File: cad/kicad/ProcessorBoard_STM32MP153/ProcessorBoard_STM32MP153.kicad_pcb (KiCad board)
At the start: 6 copper layers, 50 x 50 mm, 7 parts, among them IC401 IS43LD16320A-25BLI, J501 SFP, U201 STM32MP153CACx

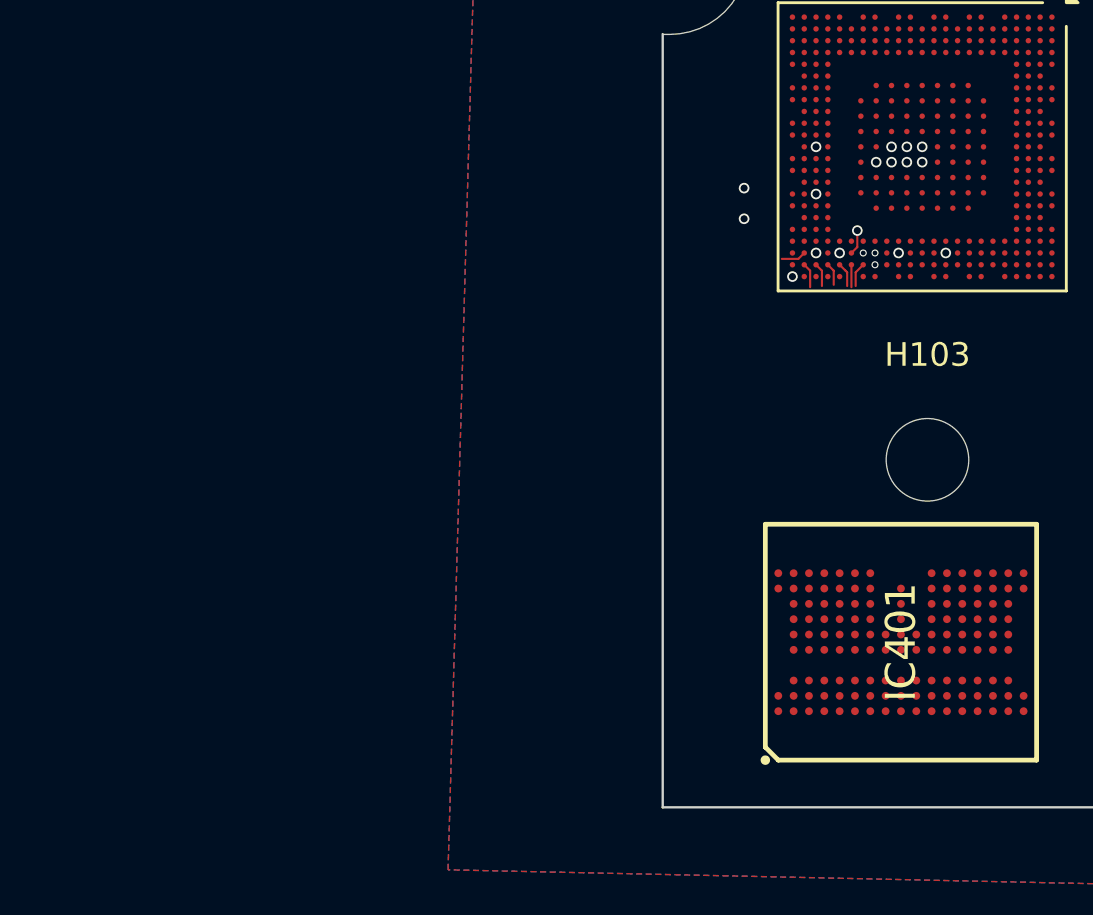
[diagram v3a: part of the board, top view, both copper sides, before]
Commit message: mpu power connections
about mpu, apparently onboard usb supply has a requirement for the onboard ldo's to be happy, so u have to tap out 2 deticated pins. and theres also a power off sequence as well???
1v8 life looking better every day, 3v3(>2v9) trenches over there
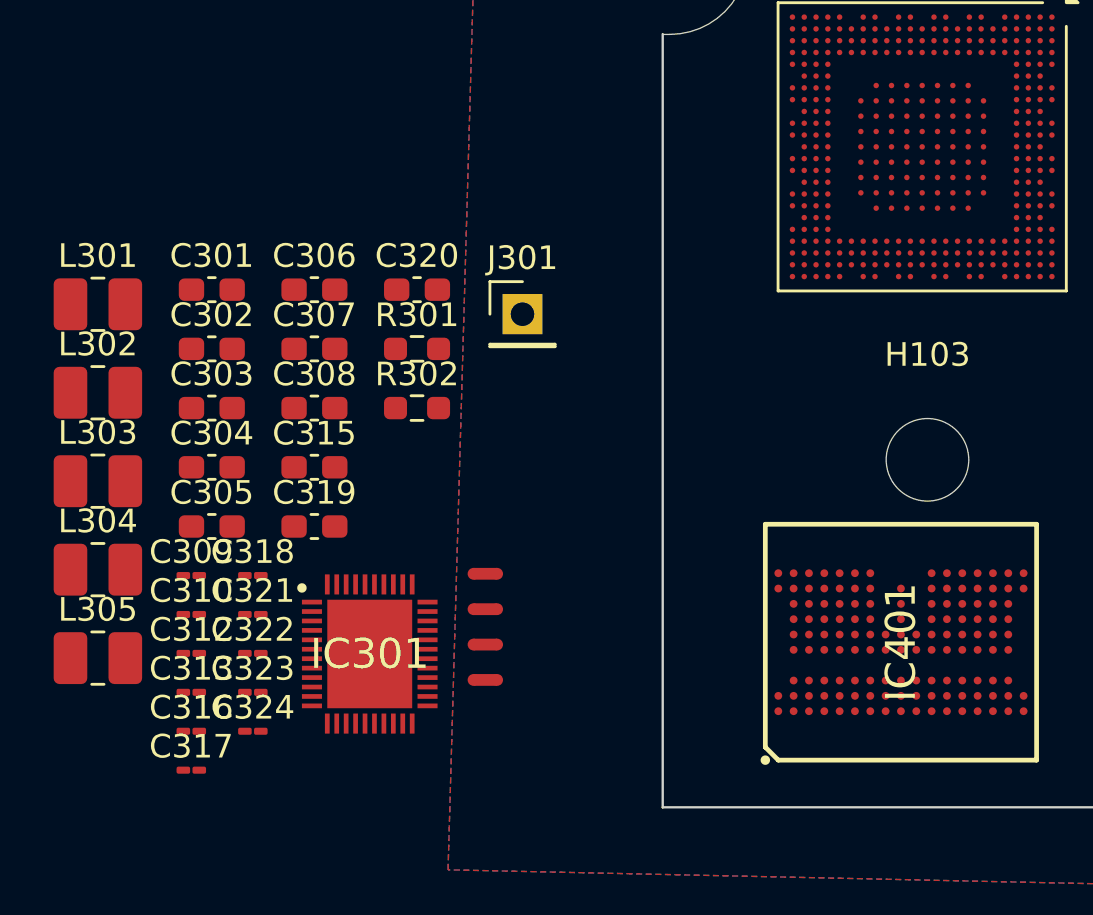
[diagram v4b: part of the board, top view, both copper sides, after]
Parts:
- added C301: 10u, Capacitor_SMD:C_0603_1608Metric_Pad1.08x0.95mm_HandSolder, F.Cu at (110.9, 98.1)
- added C302: 22u, Capacitor_SMD:C_0603_1608Metric_Pad1.08x0.95mm_HandSolder, F.Cu at (110.9, 100.6)
- added C303: 10u, Capacitor_SMD:C_0603_1608Metric_Pad1.08x0.95mm_HandSolder, F.Cu at (110.9, 103.1)
- added C304: 22u, Capacitor_SMD:C_0603_1608Metric_Pad1.08x0.95mm_HandSolder, F.Cu at (110.9, 105.6)
- added C305: 10u, Capacitor_SMD:C_0603_1608Metric_Pad1.08x0.95mm_HandSolder, F.Cu at (110.9, 108.1)
- added C306: 22u, Capacitor_SMD:C_0603_1608Metric_Pad1.08x0.95mm_HandSolder, F.Cu at (115.2, 98.1)
- added C307: 10u, Capacitor_SMD:C_0603_1608Metric_Pad1.08x0.95mm_HandSolder, F.Cu at (115.2, 100.6)
- added C308: 22u, Capacitor_SMD:C_0603_1608Metric_Pad1.08x0.95mm_HandSolder, F.Cu at (115.2, 103.1)
- added C309: 1u, Capacitor_SMD:C_01005_0402Metric_Pad0.57x0.30mm_HandSolder, F.Cu at (110.0, 110.2)
- added C310: 4.7u, Capacitor_SMD:C_01005_0402Metric_Pad0.57x0.30mm_HandSolder, F.Cu at (110.0, 111.8)
- added C312: 1u, Capacitor_SMD:C_01005_0402Metric_Pad0.57x0.30mm_HandSolder, F.Cu at (110.0, 113.5)
- added C313: 4.7u, Capacitor_SMD:C_01005_0402Metric_Pad0.57x0.30mm_HandSolder, F.Cu at (110.0, 115.1)
- added C315: 10u, Capacitor_SMD:C_0603_1608Metric_Pad1.08x0.95mm_HandSolder, F.Cu at (115.2, 105.6)
- added C316: 1u, Capacitor_SMD:C_01005_0402Metric_Pad0.57x0.30mm_HandSolder, F.Cu at (110.0, 116.8)
- added C317: 1u, Capacitor_SMD:C_01005_0402Metric_Pad0.57x0.30mm_HandSolder, F.Cu at (110.0, 118.4)
- added C318: 4.7u, Capacitor_SMD:C_01005_0402Metric_Pad0.57x0.30mm_HandSolder, F.Cu at (112.6, 110.2)
- added C319: 10u, Capacitor_SMD:C_0603_1608Metric_Pad1.08x0.95mm_HandSolder, F.Cu at (115.2, 108.1)
- added C320: 10u, Capacitor_SMD:C_0603_1608Metric_Pad1.08x0.95mm_HandSolder, F.Cu at (119.6, 98.1)
- added C321: 1u, Capacitor_SMD:C_01005_0402Metric_Pad0.57x0.30mm_HandSolder, F.Cu at (112.6, 111.8)
- added C322: 4.7u, Capacitor_SMD:C_01005_0402Metric_Pad0.57x0.30mm_HandSolder, F.Cu at (112.6, 113.5)
- added C323: 4.7u, Capacitor_SMD:C_01005_0402Metric_Pad0.57x0.30mm_HandSolder, F.Cu at (112.6, 115.1)
- added C324: 1u, Capacitor_SMD:C_01005_0402Metric_Pad0.57x0.30mm_HandSolder, F.Cu at (112.6, 116.8)
- added IC301: STPMIC1BPQR, __WM_Local:QFN40P500X600X80-45N-D, F.Cu at (117.6, 113.5)
- added J301: Conn_01x01_Pin, Connector_PinHeader_2.54mm:PinHeader_1x01_P2.54mm_Vertical, F.Cu at (124.1, 99.1)
- added L301: 1u, Inductor_SMD:L_1008_2520Metric_Pad1.43x2.20mm_HandSolder, F.Cu at (106.1, 98.7)
- added L302: 1u, Inductor_SMD:L_1008_2520Metric_Pad1.43x2.20mm_HandSolder, F.Cu at (106.1, 102.4)
- added L303: 1u, Inductor_SMD:L_1008_2520Metric_Pad1.43x2.20mm_HandSolder, F.Cu at (106.1, 106.2)
- added L304: 1u, Inductor_SMD:L_1008_2520Metric_Pad1.43x2.20mm_HandSolder, F.Cu at (106.1, 109.9)
- added L305: 1u, Inductor_SMD:L_1008_2520Metric_Pad1.43x2.20mm_HandSolder, F.Cu at (106.1, 113.7)
- added NT301: NetTie_2, NetTie:NetTie-2_SMD_Pad0.5mm, F.Cu at (122.5, 110.1)
- added NT302: NetTie_2, NetTie:NetTie-2_SMD_Pad0.5mm, F.Cu at (122.5, 111.6)
- added NT303: NetTie_2, NetTie:NetTie-2_SMD_Pad0.5mm, F.Cu at (122.5, 113.1)
- added NT304: NetTie_2, NetTie:NetTie-2_SMD_Pad0.5mm, F.Cu at (122.5, 114.6)
- added R301: 3090, Resistor_SMD:R_0603_1608Metric_Pad0.98x0.95mm_HandSolder, F.Cu at (119.6, 100.6)
- added R302: 3090, Resistor_SMD:R_0603_1608Metric_Pad0.98x0.95mm_HandSolder, F.Cu at (119.6, 103.1)
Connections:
- U201 pad 1G2: unconnected-(U201-VDD_ANA-Pad1G2) -> /V_{dd_core}
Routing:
- net GND: track 1.05 -> 0.00 mm, vias 13 -> 0
- net unconnected-(U201-DDR_DQ26-PadAB21): track 1.05 -> 0.00 mm
- net unconnected-(U201-DDR_DQS3P-PadAB22): track 1.05 -> 0.00 mm
- net unconnected-(U201-DDR_DQS1P-PadU22): track 1.03 -> 0.00 mm
- net unconnected-(U201-DDR_DQ14-PadW22): track 1.03 -> 0.00 mm
- net unconnected-(U201-DDR_DQ31-PadAA22): track 1.00 -> 0.00 mm
- net unconnected-(U201-DDR_DQ25-PadY22): track 0.95 -> 0.00 mm
- net unconnected-(U201-DDR_DQM1-PadV22): track 0.95 -> 0.00 mm
- net unconnected-(U201-DDR_DQ8-PadT21): track 0.88 -> 0.00 mm, vias 1 -> 0
- net unconnected-(U201-DDR_DQ9-PadU21): track 0.85 -> 0.00 mm, vias 1 -> 0
- net unconnected-(U201-DDR_DQ11-PadW21): vias 1 -> 0
- net unconnected-(U201-DDR_DQ10-PadT22): vias 1 -> 0
- net /V_{dd_core}: vias 3 -> 0

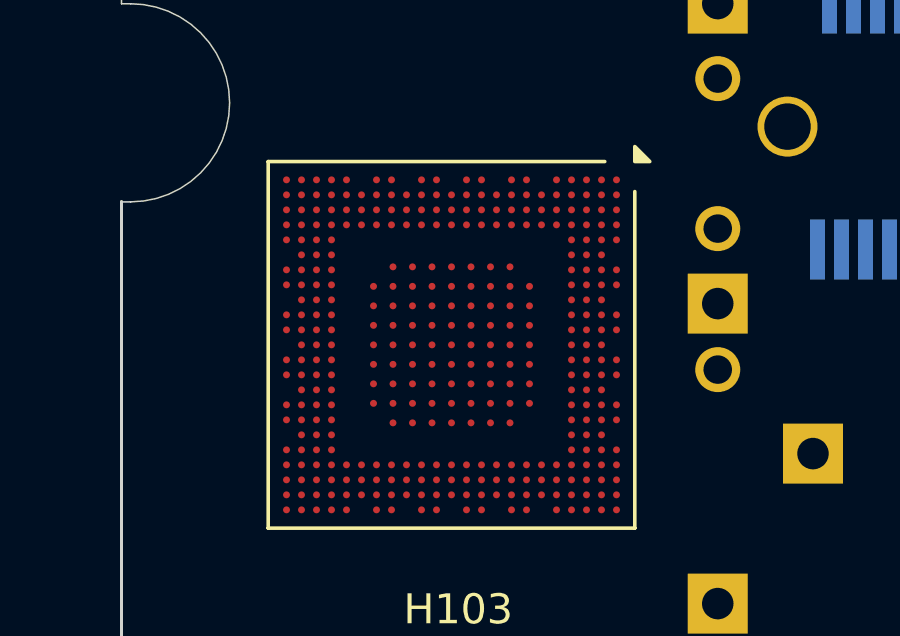
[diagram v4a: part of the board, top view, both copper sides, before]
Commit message: mr przudent get down
a thrid DDR voltage requirement has hit the power plane.
the cost of 11$ ram is apparently 3 distinct power nets :( .
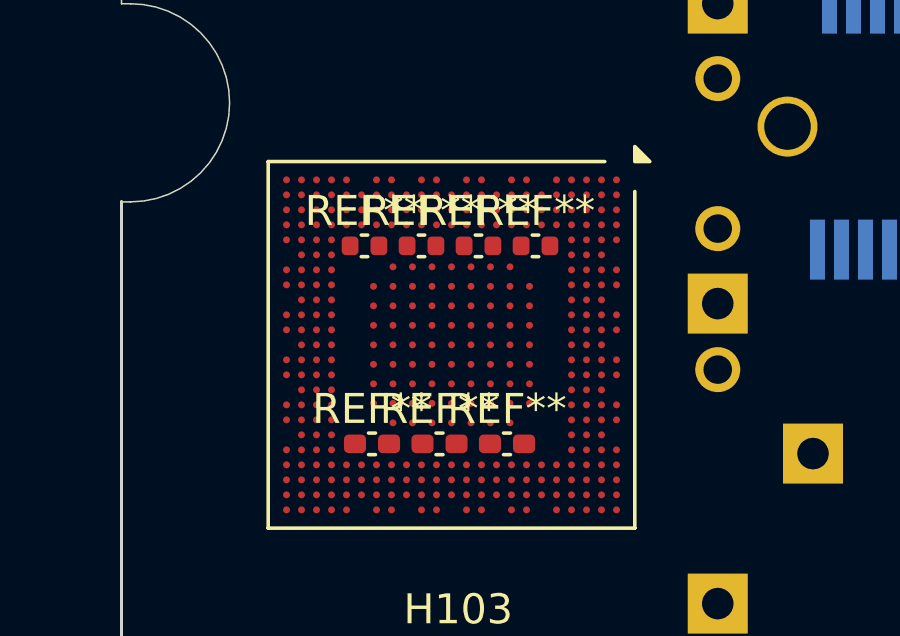
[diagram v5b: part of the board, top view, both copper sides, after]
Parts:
- added REF**: C_0402_1005Metric, Capacitor_SMD:C_0402_1005Metric, F.Cu at (143.8, 88.7)
- added REF**: C_0402_1005Metric_Pad0.74x0.62mm_HandSolder, Capacitor_SMD:C_0402_1005Metric_Pad0.74x0.62mm_HandSolder, F.Cu at (142.8, 95.3)
- added REF**: C_0402_1005Metric, Capacitor_SMD:C_0402_1005Metric, F.Cu at (141.9, 88.7)
- added REF**: C_0402_1005Metric_Pad0.74x0.62mm_HandSolder, Capacitor_SMD:C_0402_1005Metric_Pad0.74x0.62mm_HandSolder, F.Cu at (138.3, 95.3)
- added REF**: C_0402_1005Metric, Capacitor_SMD:C_0402_1005Metric, F.Cu at (140.0, 88.7)
- added REF**: C_0402_1005Metric, Capacitor_SMD:C_0402_1005Metric, F.Cu at (138.1, 88.7)
- added REF**: C_0402_1005Metric_Pad0.74x0.62mm_HandSolder, Capacitor_SMD:C_0402_1005Metric_Pad0.74x0.62mm_HandSolder, F.Cu at (140.6, 95.3)

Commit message: is this tuff
most datasheets from LCSC are "not for public release"
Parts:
- removed H103: MountingHole, MountingHole:MountingHole_3.5mm
- removed REF** (x4): C_0402_1005Metric, Capacitor_SMD:C_0402_1005Metric
- removed REF** (x3): C_0402_1005Metric_Pad0.74x0.62mm_HandSolder, Capacitor_SMD:C_0402_1005Metric_Pad0.74x0.62mm_HandSolder
- added C201: 100n, Capacitor_SMD:C_0402_1005Metric_Pad0.74x0.62mm_HandSolder, F.Cu at (111.7, 96.7)
- added C202: 1u, Capacitor_SMD:C_0402_1005Metric_Pad0.74x0.62mm_HandSolder, F.Cu at (106.1, 81.3)
- added C203: 1u, Capacitor_SMD:C_0402_1005Metric_Pad0.74x0.62mm_HandSolder, F.Cu at (106.1, 82.9)
- added C204: 1u, Capacitor_SMD:C_0402_1005Metric_Pad0.74x0.62mm_HandSolder, F.Cu at (106.1, 84.6)
- added C205: 1u, Capacitor_SMD:C_0402_1005Metric_Pad0.74x0.62mm_HandSolder, F.Cu at (106.1, 86.2)
- added C206: 1u, Capacitor_SMD:C_0402_1005Metric_Pad0.74x0.62mm_HandSolder, F.Cu at (106.1, 87.9)
- added C207: 1u, Capacitor_SMD:C_0402_1005Metric_Pad0.74x0.62mm_HandSolder, F.Cu at (106.1, 89.5)
- added C208: 1u, Capacitor_SMD:C_0402_1005Metric_Pad0.74x0.62mm_HandSolder, F.Cu at (108.7, 79.6)
- added C209: 1u, Capacitor_SMD:C_0402_1005Metric_Pad0.74x0.62mm_HandSolder, F.Cu at (108.7, 81.3)
- added C210: 1u, Capacitor_SMD:C_0402_1005Metric_Pad0.74x0.62mm_HandSolder, F.Cu at (108.7, 82.9)
- added C211: 1u, Capacitor_SMD:C_0402_1005Metric_Pad0.74x0.62mm_HandSolder, F.Cu at (108.7, 84.6)
- added C212: 1u, Capacitor_SMD:C_0402_1005Metric_Pad0.74x0.62mm_HandSolder, F.Cu at (108.7, 86.2)
- added C213: 1u, Capacitor_SMD:C_0402_1005Metric_Pad0.74x0.62mm_HandSolder, F.Cu at (108.7, 87.9)
- added C214: 1u, Capacitor_SMD:C_0402_1005Metric_Pad0.74x0.62mm_HandSolder, F.Cu at (108.7, 89.5)
- added C215: 1u, Capacitor_SMD:C_0402_1005Metric_Pad0.74x0.62mm_HandSolder, F.Cu at (111.3, 79.6)
- added C216: 1u, Capacitor_SMD:C_0402_1005Metric_Pad0.74x0.62mm_HandSolder, F.Cu at (111.3, 81.3)
- added C217: 1u, Capacitor_SMD:C_0402_1005Metric_Pad0.74x0.62mm_HandSolder, F.Cu at (111.3, 82.9)
- added C218: 1u, Capacitor_SMD:C_0402_1005Metric_Pad0.74x0.62mm_HandSolder, F.Cu at (111.3, 84.6)
- added C219: 1n, Capacitor_SMD:C_0402_1005Metric_Pad0.74x0.62mm_HandSolder, F.Cu at (111.3, 86.2)
- added C220: 1n, Capacitor_SMD:C_0402_1005Metric_Pad0.74x0.62mm_HandSolder, F.Cu at (111.3, 87.9)
- added C221: 1u, Capacitor_SMD:C_0402_1005Metric_Pad0.74x0.62mm_HandSolder, F.Cu at (111.3, 89.5)
- added C222: 1u, Capacitor_SMD:C_0402_1005Metric_Pad0.74x0.62mm_HandSolder, F.Cu at (113.9, 79.6)
- added C223: 1u, Capacitor_SMD:C_0402_1005Metric_Pad0.74x0.62mm_HandSolder, F.Cu at (113.9, 81.3)
- added C224: 100n, Capacitor_SMD:C_0402_1005Metric_Pad0.74x0.62mm_HandSolder, F.Cu at (111.7, 98.7)
- added C225: 100n, Capacitor_SMD:C_0402_1005Metric_Pad0.74x0.62mm_HandSolder, F.Cu at (114.1, 83.1)
- added C227: 100n, Capacitor_SMD:C_0402_1005Metric_Pad0.74x0.62mm_HandSolder, F.Cu at (114.1, 85.1)
- added C228: 100n, Capacitor_SMD:C_0402_1005Metric_Pad0.74x0.62mm_HandSolder, F.Cu at (111.7, 100.6)
- added C229: 100n, Capacitor_SMD:C_0402_1005Metric_Pad0.74x0.62mm_HandSolder, F.Cu at (114.1, 87.1)
- added C401: 100n, Capacitor_SMD:C_0402_1005Metric_Pad0.74x0.62mm_HandSolder, F.Cu at (114.6, 109.3)
- added C402: 100n, Capacitor_SMD:C_0402_1005Metric_Pad0.74x0.62mm_HandSolder, F.Cu at (114.6, 111.3)
- added C403: 100n, Capacitor_SMD:C_0402_1005Metric_Pad0.74x0.62mm_HandSolder, F.Cu at (114.6, 113.3)
- added C404: 100n, Capacitor_SMD:C_0402_1005Metric_Pad0.74x0.62mm_HandSolder, F.Cu at (114.6, 115.2)
- added J201: Conn_01x03_Pin, Connector_PinHeader_1.27mm:PinHeader_1x03_P1.27mm_Vertical, F.Cu at (117.3, 90.5)
- added R201: 47k, Resistor_SMD:R_0603_1608Metric_Pad0.98x0.95mm_HandSolder, F.Cu at (117.4, 80.1)
- added R202: 47k, Resistor_SMD:R_0603_1608Metric_Pad0.98x0.95mm_HandSolder, F.Cu at (117.4, 82.6)
- added R203: 3090, Resistor_SMD:R_0603_1608Metric_Pad0.98x0.95mm_HandSolder, F.Cu at (117.4, 85.1)
- added R204: 47k, Resistor_SMD:R_0603_1608Metric_Pad0.98x0.95mm_HandSolder, F.Cu at (117.4, 87.6)
- added R205: 240, Capacitor_SMD:C_0402_1005Metric_Pad0.74x0.62mm_HandSolder, F.Cu at (110.0, 91.3)
- added R206: 10k, Capacitor_SMD:C_0402_1005Metric_Pad0.74x0.62mm_HandSolder, F.Cu at (142.8, 84.5)
- added R207: 1k, Capacitor_SMD:C_0402_1005Metric_Pad0.74x0.62mm_HandSolder, F.Cu at (142.8, 86.4)
- added R208: 10, Resistor_SMD:R_0402_1005Metric_Pad0.72x0.64mm_HandSolder, F.Cu at (142.8, 85.4)
- added R401: 240, Capacitor_SMD:C_0402_1005Metric_Pad0.74x0.62mm_HandSolder, F.Cu at (110.4, 115.2)
- added TP201: TestPoint, TestPoint:TestPoint_Pad_D1.5mm, F.Cu at (106.6, 92.1)
- added X201: ECS-3225MVQ-240-CN-TR, Package_DFN_QFN:CDFN-4_2.5x3.2mm_P2.1mm, F.Cu at (138.8, 85.8)
- C309, C310, C312, C313, C316, C317, C318, C321, C322, C323, C324: footprint Capacitor_SMD:C_01005_0402Metric_Pad0.57x0.30mm_HandSolder -> Capacitor_SMD:C_0402_1005Metric_Pad0.74x0.62mm_HandSolder
- IC301: moved to B.Cu
- J501: footprint Connector:Connector_SFP_and_Cage -> __WM_Local:Connector_SFP_and_Cage; moved to F.Cu
- R301, R302: value 3090 -> 1.2k
- moved J301 61.0 mm to (163.5, 145.6)
- moved C307 56.2 mm to (160.1, 134.5)
- moved C312 56.2 mm to (154.8, 147.4)
- moved C313 56.2 mm to (154.8, 149.1)
- moved C319 56.2 mm to (160.1, 142.0)
- moved R301 56.2 mm to (164.4, 134.5)
- moved C306 56.2 mm to (160.1, 132.0)
- moved C308 56.2 mm to (160.1, 137.0)
- moved C309 56.2 mm to (154.8, 144.1)
- moved C310 56.2 mm to (154.8, 145.8)
- moved C315 56.2 mm to (160.1, 139.5)
- moved C316 56.2 mm to (154.8, 150.7)
- moved C317 56.2 mm to (154.8, 152.3)
- moved C320 56.2 mm to (164.4, 132.0)
- moved C322 56.2 mm to (157.4, 147.4)
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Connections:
- net /Power MPU/INTn renamed /INTn
- net /Power MPU/RSTn renamed /RSTn
- net /Power MPU/SCL renamed /SCL
- net /Power MPU/SDA renamed /SDA
- net /Power MPU/WakeUp renamed /WakeUp
- C319 pad 1: /V_{dd_core} -> /V_{dd_IO}
- C320 pad 1: /V_{dd_DDR2} -> /V_{dd_DDR1}
- IC301 pad 13: /V_{dd_core} -> /V_{dd_IO}
- IC301 pad 14: /V_{dd_DDR2} -> /V_{dd_DDR1}
- IC301 pad 44: /Power MPU/PwrCtrl -> /PwrCtrl
- IC401 pad B5: unconnected-(IC401-VDD2_1-PadB5) -> /V_{dd_DDRQ}
- IC401 pad B6: unconnected-(IC401-VDD1_1-PadB6) -> /V_{dd_DDR1}
- IC401 pad C1: unconnected-(IC401-VDD1_2-PadC1) -> /V_{dd_DDR1}
- IC401 pad C10: unconnected-(IC401-VDDQ_2-PadC10) -> /V_{dd_DDRQ}
- IC401 pad C2: unconnected-(IC401-VSS_1-PadC2) -> GND
- IC401 pad C5: unconnected-(IC401-VSS_2-PadC5) -> GND
- IC401 pad C6: unconnected-(IC401-VSSQ_1-PadC6) -> GND
- IC401 pad C7: unconnected-(IC401-VDDQ_1-PadC7) -> /V_{dd_DDRQ}
- IC401 pad C9: unconnected-(IC401-VSSQ_2-PadC9) -> GND
- IC401 pad D1: unconnected-(IC401-VSS_3-PadD1) -> GND
- IC401 pad D10: unconnected-(IC401-VSSQ_3-PadD10) -> GND
- IC401 pad D2: unconnected-(IC401-VDD2_2-PadD2) -> /V_{dd_DDRQ}
- IC401 pad D3: unconnected-(IC401-ZQ-PadD3) -> Net-(IC401-ZQ)
- IC401 pad D5: unconnected-(IC401-VDDQ_3-PadD5) -> /V_{dd_DDRQ}
- IC401 pad E1: unconnected-(IC401-VSSCA_1-PadE1) -> GND
- IC401 pad E10: unconnected-(IC401-VSSQ_4-PadE10) -> GND
- IC401 pad E2: unconnected-(IC401-CA9-PadE2) -> /a9
- IC401 pad E3: unconnected-(IC401-CA8-PadE3) -> /a8
- IC401 pad E8: unconnected-(IC401-DQ15-PadE8) -> /d15
- IC401 pad E9: unconnected-(IC401-VDDQ_4-PadE9) -> /V_{dd_DDRQ}
- IC401 pad F1: unconnected-(IC401-VDDCA_1-PadF1) -> /V_{dd_DDRQ}
- IC401 pad F10: unconnected-(IC401-VDDQ_5-PadF10) -> /V_{dd_DDRQ}
- IC401 pad F2: unconnected-(IC401-CA6-PadF2) -> /a6
- IC401 pad F3: unconnected-(IC401-CA7-PadF3) -> /a7
- IC401 pad F5: unconnected-(IC401-VSSQ_5-PadF5) -> GND
- IC401 pad F6: unconnected-(IC401-DQ11-PadF6) -> /d11
- IC401 pad F7: unconnected-(IC401-DQ13-PadF7) -> /d13
- IC401 pad F8: unconnected-(IC401-DQ14-PadF8) -> /d14
- IC401 pad F9: unconnected-(IC401-DQ12-PadF9) -> /d12
- IC401 pad G1: unconnected-(IC401-VDD2_3-PadG1) -> /V_{dd_DDRQ}
- IC401 pad G10: unconnected-(IC401-VSSQ_6-PadG10) -> GND
- IC401 pad G2: unconnected-(IC401-CA5-PadG2) -> /a5
- IC401 pad G3: unconnected-(IC401-VREF(CA)-PadG3) -> /V_{DDR_ref}
- IC401 pad G5: unconnected-(IC401-DQS1#-PadG5) -> /s1_N
- IC401 pad G6: unconnected-(IC401-DQS1-PadG6) -> /s1_P
- IC401 pad G7: unconnected-(IC401-DQ10-PadG7) -> /d10
- IC401 pad G8: unconnected-(IC401-DQ9-PadG8) -> /d9
- IC401 pad G9: unconnected-(IC401-DQ8-PadG9) -> /d8
- IC401 pad H1: unconnected-(IC401-VDDCA_2-PadH1) -> /V_{dd_DDRQ}
- IC401 pad H2: unconnected-(IC401-VSS_4-PadH2) -> GND
- IC401 pad H3: unconnected-(IC401-CK#-PadH3) -> /CLK_N
- IC401 pad H5: unconnected-(IC401-DM1-PadH5) -> /m1
- IC401 pad H6: unconnected-(IC401-VDDQ_6-PadH6) -> /V_{dd_DDRQ}
- IC401 pad J1: unconnected-(IC401-VSSCA_2-PadJ1) -> GND
- IC401 pad J3: unconnected-(IC401-CK-PadJ3) -> /CLK_P
- IC401 pad J5: unconnected-(IC401-VSSQ_7-PadJ5) -> GND
- IC401 pad J6: unconnected-(IC401-VDDQ_7-PadJ6) -> /V_{dd_DDRQ}
- IC401 pad J7: unconnected-(IC401-VDD2_4-PadJ7) -> /V_{dd_DDRQ}
- IC401 pad J8: unconnected-(IC401-VSS_5-PadJ8) -> GND
- IC401 pad J9: unconnected-(IC401-VREF(DQ)-PadJ9) -> /V_{DDR_ref}
- IC401 pad K1: unconnected-(IC401-CKE-PadK1) -> /CKE
- IC401 pad K5: unconnected-(IC401-DM0-PadK5) -> /m0
- IC401 pad K6: unconnected-(IC401-VDDQ_8-PadK6) -> /V_{dd_DDRQ}
- IC401 pad L1: unconnected-(IC401-CS#-PadL1) -> /CSn
- IC401 pad L10: unconnected-(IC401-VSSQ_8-PadL10) -> GND
- IC401 pad L5: unconnected-(IC401-DQS0#-PadL5) -> /s0_N
- IC401 pad L6: unconnected-(IC401-DQS0-PadL6) -> /s0_P
- IC401 pad L7: unconnected-(IC401-DQ5-PadL7) -> /d5
- IC401 pad L8: unconnected-(IC401-DQ6-PadL8) -> /d6
- IC401 pad L9: unconnected-(IC401-DQ7-PadL9) -> /d7
- IC401 pad M1: unconnected-(IC401-CA4-PadM1) -> /a4
- IC401 pad M10: unconnected-(IC401-VDDQ_9-PadM10) -> /V_{dd_DDRQ}
- IC401 pad M2: unconnected-(IC401-CA3-PadM2) -> /a3
- IC401 pad M3: unconnected-(IC401-CA2-PadM3) -> /a2
- IC401 pad M5: unconnected-(IC401-VSSQ_9-PadM5) -> GND
- IC401 pad M6: unconnected-(IC401-DQ4-PadM6) -> /d4
- IC401 pad M7: unconnected-(IC401-DQ2-PadM7) -> /d2
- IC401 pad M8: unconnected-(IC401-DQ1-PadM8) -> /d1
- IC401 pad M9: unconnected-(IC401-DQ3-PadM9) -> /d3
- IC401 pad N1: unconnected-(IC401-VSSCA_3-PadN1) -> GND
- IC401 pad N10: unconnected-(IC401-VSSQ_10-PadN10) -> GND
- IC401 pad N2: unconnected-(IC401-VDDCA_3-PadN2) -> /V_{dd_DDRQ}
- IC401 pad N3: unconnected-(IC401-CA1-PadN3) -> /a1
- IC401 pad N8: unconnected-(IC401-DQ0-PadN8) -> /d0
- IC401 pad N9: unconnected-(IC401-VDDQ_10-PadN9) -> /V_{dd_DDRQ}
- IC401 pad P1: unconnected-(IC401-VSS_6-PadP1) -> GND
- IC401 pad P10: unconnected-(IC401-VSSQ_11-PadP10) -> GND
- IC401 pad P2: unconnected-(IC401-VDD2_5-PadP2) -> /V_{dd_DDRQ}
- IC401 pad P3: unconnected-(IC401-CA0-PadP3) -> /a0
- IC401 pad P5: unconnected-(IC401-VDDQ_11-PadP5) -> /V_{dd_DDRQ}
- IC401 pad R1: unconnected-(IC401-VDD1_3-PadR1) -> /V_{dd_DDR1}
- IC401 pad R10: unconnected-(IC401-VDDQ_13-PadR10) -> /V_{dd_DDRQ}
- IC401 pad R2: unconnected-(IC401-VSS_7-PadR2) -> GND
- IC401 pad R5: unconnected-(IC401-VSS_8-PadR5) -> GND
- IC401 pad R6: unconnected-(IC401-VSSQ_12-PadR6) -> GND
- IC401 pad R7: unconnected-(IC401-VDDQ_12-PadR7) -> /V_{dd_DDRQ}
- IC401 pad R9: unconnected-(IC401-VSSQ_13-PadR9) -> GND
- IC401 pad T5: unconnected-(IC401-VDD2_6-PadT5) -> /V_{dd_DDRQ}
- IC401 pad T6: unconnected-(IC401-VDD1_4-PadT6) -> /V_{dd_DDR1}
- U201 pad 1F1: unconnected-(U201-VBAT-Pad1F1) -> /V_{dd_IO}
- U201 pad 1F3: unconnected-(U201-VDD-Pad1F3) -> /V_{dd_IO}
- U201 pad 1G2: /V_{dd_core} -> /V_{dd_IO}
- U201 pad 1G4: unconnected-(U201-VDD-Pad1G4) -> /V_{dd_IO}
- U201 pad 1H1: unconnected-(U201-VDDA-Pad1H1) -> /V_{ddA}
- U201 pad 1H3: unconnected-(U201-VDD-Pad1H3) -> /V_{dd_IO}
- U201 pad 1H5: unconnected-(U201-VDD-Pad1H5) -> /V_{dd_IO}
- U201 pad 1J2: unconnected-(U201-VDD-Pad1J2) -> /V_{dd_IO}
- U201 pad 1J4: unconnected-(U201-VDD-Pad1J4) -> /V_{dd_IO}
- U201 pad 1J6: unconnected-(U201-VDD-Pad1J6) -> /V_{dd_IO}
- U201 pad AA15: Net-(U201-VDD3V3_USBFS) -> /V_{dd_USB}
- U201 pad AA17: Net-(U201-VDD3V3_USBFS) -> /V_{dd_USB}
- U201 pad AB13: unconnected-(U201-BYPASS_REG1V8-PadAB13) -> GND
- U201 pad AB14: unconnected-(U201-VDDA1V8_REG-PadAB14) -> Net-(U201-VDDA1V8_REG)
- U201 pad AB15: unconnected-(U201-VDDA1V1_REG-PadAB15) -> Net-(U201-VDDA1V1_REG)
- U201 pad AC20: unconnected-(U201-DDR_VREF-PadAC20) -> /V_{DDR_ref}
- U201 pad D20: unconnected-(U201-DDR_RESETN-PadD20) -> /RESETn
- U201 pad E20: unconnected-(U201-DDR_A7-PadE20) -> /a7
- U201 pad E21: unconnected-(U201-DDR_DQ3-PadE21) -> /d3
- U201 pad E22: unconnected-(U201-DDR_DQ0-PadE22) -> /d0
- U201 pad F22: unconnected-(U201-DDR_DQ1-PadF22) -> /d1
- U201 pad G20: unconnected-(U201-DDR_A9-PadG20) -> /a9
- U201 pad G21: unconnected-(U201-DDR_DQ7-PadG21) -> /d7
- U201 pad G22: unconnected-(U201-DDR_DQS0P-PadG22) -> /s0_P
- U201 pad G23: unconnected-(U201-DDR_DQS0N-PadG23) -> /s0_N
- U201 pad H20: unconnected-(U201-DDR_A5-PadH20) -> /a5
- U201 pad H21: unconnected-(U201-DDR_DQ2-PadH21) -> /d2
- U201 pad H22: unconnected-(U201-DDR_DQ6-PadH22) -> /d6
- U201 pad H23: unconnected-(U201-DDR_DQM0-PadH23) -> /m0
- U201 pad J20: unconnected-(U201-DDR_A2-PadJ20) -> /a2
- U201 pad J21: unconnected-(U201-DDR_DQ4-PadJ21) -> /d4
- U201 pad J22: unconnected-(U201-DDR_DQ5-PadJ22) -> /d5
- U201 pad K22: unconnected-(U201-DDR_A3-PadK22) -> /a3
- U201 pad K23: unconnected-(U201-DDR_ZQ-PadK23) -> Net-(U201-DDR_ZQ)
- U201 pad L20: unconnected-(U201-DDR_A0-PadL20) -> /a0
- U201 pad L22: unconnected-(U201-DDR_ODT-PadL22) -> /ODT
- U201 pad L23: unconnected-(U201-DDR_BA0-PadL23) -> /b0
- U201 pad M2: unconnected-(U201-BOOT2-PadM2) -> /MPU/Boot2
- U201 pad M20: unconnected-(U201-DDR_WEN-PadM20) -> /WEN
- U201 pad M21: unconnected-(U201-DDR_BA2-PadM21) -> /b2
- U201 pad M22: unconnected-(U201-DDR_CSN-PadM22) -> /CSn
- U201 pad M3: unconnected-(U201-NRST-PadM3) -> Net-(U201-NRST)
- U201 pad M4: unconnected-(U201-NRST_CORE-PadM4) -> Net-(U201-NRST_CORE)
- U201 pad N1: unconnected-(U201-BOOT0-PadN1) -> /MPU/Boot0
- U201 pad N20: unconnected-(U201-DDR_CASN-PadN20) -> /CASn
- U201 pad N21: unconnected-(U201-DDR_RASN-PadN21) -> /RASn
- U201 pad N22: unconnected-(U201-DDR_CLKP-PadN22) -> /CLK_P
- U201 pad N23: unconnected-(U201-DDR_CLKN-PadN23) -> /CLK_N
- U201 pad N3: unconnected-(U201-PWR_LP-PadN3) -> Net-(U201-PWR_LP)
- U201 pad N4: unconnected-(U201-BOOT1-PadN4) -> /MPU/Boot1
- U201 pad P1: unconnected-(U201-PH0-PadP1) -> /MPU/OSC_HSE_in
- U201 pad P2: unconnected-(U201-PH1-PadP2) -> /MPU/OSC_HSE_out
- U201 pad P22: unconnected-(U201-DDR_A1-PadP22) -> /a1
- U201 pad R2: unconnected-(U201-PWR_ON-PadR2) -> /PwrCtrl
- U201 pad R3: unconnected-(U201-PDR_ON-PadR3) -> /V_{dd_IO}
- U201 pad R4: unconnected-(U201-VREF+-PadR4) -> /V_{ddA}
- U201 pad T20: unconnected-(U201-DDR_CKE-PadT20) -> /CKE
- U201 pad T21: unconnected-(U201-DDR_DQ8-PadT21) -> /d8
- U201 pad T22: unconnected-(U201-DDR_DQ10-PadT22) -> /d10
- U201 pad T23: unconnected-(U201-DDR_DQ13-PadT23) -> /d13
- U201 pad T3: unconnected-(U201-PDR_ON_CORE-PadT3) -> /V_{dd_IO}
- U201 pad U20: unconnected-(U201-DDR_BA1-PadU20) -> /b1
- U201 pad U21: unconnected-(U201-DDR_DQ9-PadU21) -> /d9
- U201 pad U22: unconnected-(U201-DDR_DQS1P-PadU22) -> /s1_P
- U201 pad U23: unconnected-(U201-DDR_DQS1N-PadU23) -> /s1_N
- U201 pad V20: unconnected-(U201-DDR_A4-PadV20) -> /a4
- U201 pad V22: unconnected-(U201-DDR_DQM1-PadV22) -> /m1
- U201 pad W20: unconnected-(U201-DDR_A6-PadW20) -> /a6
- U201 pad W21: unconnected-(U201-DDR_DQ11-PadW21) -> /d11
- U201 pad W22: unconnected-(U201-DDR_DQ14-PadW22) -> /d14
- U201 pad W23: unconnected-(U201-DDR_DQ12-PadW23) -> /d12
- U201 pad Y20: unconnected-(U201-DDR_A8-PadY20) -> /a8
- U201 pad Y21: unconnected-(U201-DDR_DQ15-PadY21) -> /d15

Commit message: crab company
the lion does not concern himself with radiation
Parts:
- added X501: RTL8211FS(I)-xx-xx, Package_DFN_QFN:QFN-48-1EP_6x6mm_P0.4mm_EP4.2x4.2mm, F.Cu at (170.0, 92.6)
- moved R206 9.90 mm to (133.0, 85.8)
- moved R207 9.90 mm to (133.0, 87.8)
- moved R208 9.90 mm to (133.0, 86.8)
- moved X201 2.23 mm to (136.8, 86.8)
- moved IC401 0.95 mm to (140.1, 111.0)
- moved U201 0.95 mm to (140.0, 96.8)
- moved J501 0.12 mm to (157.0, 78.4)

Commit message: yerp
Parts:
- added U601: ~, Package_TO_SOT_SMD:SOT-563, F.Cu at (170.6, 86.2)
- moved X501 1.00 mm to (170.8, 92.0)
